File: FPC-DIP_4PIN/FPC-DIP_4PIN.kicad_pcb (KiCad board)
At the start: 2 copper layers, 12.2 x 12 mm, 2 parts, among them J1 Breadboard, J2 4 Pin FPC (1mm pitch)

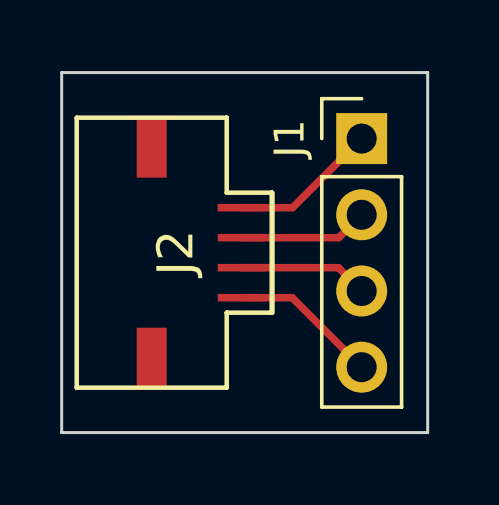
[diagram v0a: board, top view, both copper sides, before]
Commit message: Added GND pad and labels for sensirion sample flex PCBs
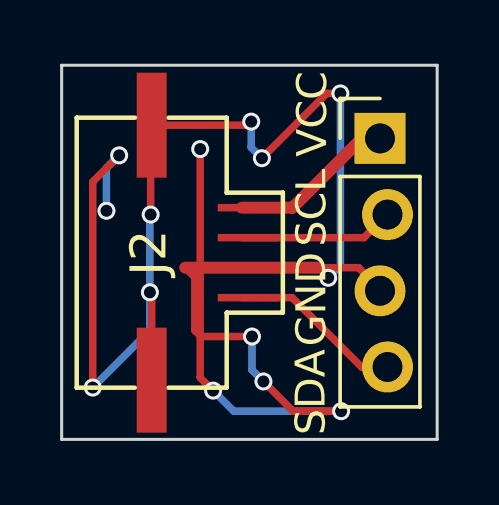
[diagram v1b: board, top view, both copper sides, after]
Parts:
- J1: value Breadboard -> Breadboard holes
- moved J1 0.61 mm to (153.1, 101.2)
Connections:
- net Net-(J1-Pad1) renamed /VCC
- net Net-(J1-Pad2) renamed /SCL
- net Net-(J1-Pad4) renamed /SDA
- J1 pad 3: Net-(J1-Pad3) -> /GND
- J2 pad 0: (no net) -> /GND
- J2 pad 3: Net-(J1-Pad3) -> /GND
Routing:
- net /GND: track 0.00 -> 68.7 mm, vias 0 -> 14
- net Net-(J1-Pad3): track 4.32 -> 0.00 mm
- net /SDA: track 4.96 -> 5.85 mm
- net /SCL: track 4.32 -> 5.17 mm
- net /VCC: track 4.95 -> 5.58 mm
- added copper zone on B.Cu, net /GND
- added copper zone on F.Cu, net /GND
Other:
- board size 12.2 x 12 mm -> 12.5 x 12.5 mm
- board text added: "FPC Adapter Sensirion Rev. 0.2"
- board text added: "GND"
- board text added: "SCL"
- board text added: "SDA"
- board text added: "VCC"
- board text removed: "FPC Adapter 1mm Pitch Rev. 0.1"
